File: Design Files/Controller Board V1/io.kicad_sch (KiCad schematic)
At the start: 16 parts, among them J1 XT30PW-F, J10 SM04B-GHS-TB_LF__SN_-, J11 SM04B-GHS-TB_LF__SN_-, J2 XT30UPB-M, J3 XT30UPB-M, J4 XT30UPB-M, J5 XT30UPB-M, J6 XT30UPB-M, J7 XT30UPB-M, J8 SM04B-GHS-TB_LF__SN_-, J9 SM04B-GHS-TB_LF__SN_-

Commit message: OOps, pushing late
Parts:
- J10, J11, J9: footprint SM04B-GHS-TB_LF__SN_-:JST_SM04B-GHS-TB_LF__SN_- -> PGA460TW:JST_SM04B-GHS-TB_LF__SN_-
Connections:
- net GPIO_0: now also J11.2; no longer J11.3
- net GPIO_1: now also J11.3; no longer J11.2
- net GPIO_2: now also J10.2; no longer J10.3
- net GPIO_3: now also J10.3; no longer J10.2
- net GPIO_4: now also J9.2; no longer J9.3
- net GPIO_5: now also J9.3; no longer J9.2
- net I2C_TypeC_SCL: now also J8.1; no longer J8.3
- net I2C_TypeC_SDA: now also J8.3; no longer J8.1
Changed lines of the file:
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@@
+		)
+	)
+	(hierarchical_label "GPIO_2"
+		(shape bidirectional)
+		(at 143.51 88.9 180)
+		(fields_autoplaced yes)
+		(effects
+			(font
+				(size 1.27 1.27)
+			)
+			(justify right)
 		)
 	)
@@
 		)
 	)
-	(hierarchical_label "GPIO_1"
-		(shape bidirectional)
-		(at 143.51 107.95 180)
-		(fields_autoplaced yes)
-		(effects
-			(font
-				(size 1.27 1.27)
-			)
-			(justify right)
-		)
-	)
-	(hierarchical_label "GPIO_0"
-		(shape bidirectional)
-		(at 143.51 110.49 180)
-		(fields_autoplaced yes)
-		(effects
-			(font
-				(size 1.27 1.27)
-			)
-			(justify right)
-		)
-	)
 	(hierarchical_label "24V_OUT"
 		(shape input)
@@
 		)
 	)
+	(hierarchical_label "GPIO_5"
+		(shape bidirectional)
+		(at 143.51 72.39 180)
+		(fields_autoplaced yes)
+		(effects
+			(font
+				(size 1.27 1.27)
+			)
+			(justify right)
+		)
+	)
 	(hierarchical_label "D_GND"
 		(shape input)
@@
 		)
 	)
-	(hierarchical_label "I2C_TypeC_SDA"
-		(shape input)
-		(at 143.51 48.26 180)
+	(hierarchical_label "GPIO_0"
+		(shape bidirectional)
+		(at 143.51 107.95 180)
 		(fields_autoplaced yes)
 		(effects
@@
 		)
 	)
-	(hierarchical_label "GPIO_2"
+	(hierarchical_label "GPIO_3"
 		(shape bidirectional)
 		(at 143.51 91.44 180)
@@
 		)
 	)
-	(hierarchical_label "GPIO_5"
-		(shape bidirectional)
-		(at 143.51 69.85 180)
-		(fields_autoplaced yes)
-		(effects
-			(font
-				(size 1.27 1.27)
-			)
-			(justify right)
-		)
-	)
-	(hierarchical_label "GPIO_3"
-		(shape bidirectional)
-		(at 143.51 88.9 180)
+	(hierarchical_label "I2C_TypeC_SCL"
+		(shape input)
+		(at 143.51 48.26 180)
 		(fields_autoplaced yes)
 		(effects
@@
 		)
 	)
+	(hierarchical_label "I2C_TypeC_SDA"
+		(shape input)
+		(at 143.51 53.34 180)
+		(fields_autoplaced yes)
+		(effects
+			(font
+				(size 1.27 1.27)
+			)
+			(justify right)
+		)
+	)
+	(hierarchical_label "GPIO_1"
+		(shape bidirectional)
+		(at 143.51 110.49 180)
+		(fields_autoplaced yes)
+		(effects
+			(font
+				(size 1.27 1.27)
+			)
+			(justify right)
+		)
+	)
 	(hierarchical_label "24_IN_PMM"
 		(shape input)
@@
 	(hierarchical_label "GPIO_4"
 		(shape bidirectional)
-		(at 143.51 72.39 180)
-		(fields_autoplaced yes)
-		(effects
-			(font
-				(size 1.27 1.27)
-			)
-			(justify right)
-		)
-	)
-	(hierarchical_label "I2C_TypeC_SCL"
-		(shape input)
-		(at 143.51 53.34 180)
+		(at 143.51 69.85 180)
 		(fields_autoplaced yes)
 		(effects
@@
 			)
 		)
-		(property "Footprint" "SM04B-GHS-TB_LF__SN_-:JST_SM04B-GHS-TB_LF__SN_-"
+		(property "Footprint" "PGA460TW:JST_SM04B-GHS-TB_LF__SN_-"
 			(at 153.67 91.44 0)
 			(effects
@@
 			)
 		)
-		(property "Footprint" "SM04B-GHS-TB_LF__SN_-:JST_SM04B-GHS-TB_LF__SN_-"
+		(property "Footprint" "PGA460TW:JST_SM04B-GHS-TB_LF__SN_-"
 			(at 153.67 110.49 0)
 			(effects
@@
 			)
 		)
-		(property "Footprint" "SM04B-GHS-TB_LF__SN_-:JST_SM04B-GHS-TB_LF__SN_-"
+		(property "Footprint" "PGA460TW:JST_SM04B-GHS-TB_LF__SN_-"
 			(at 153.67 72.39 0)
 			(effects

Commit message: board
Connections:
- net D_GND is gone; now on net P_GND: J10.4, J11.4, J8.2, J8.4, J9.4

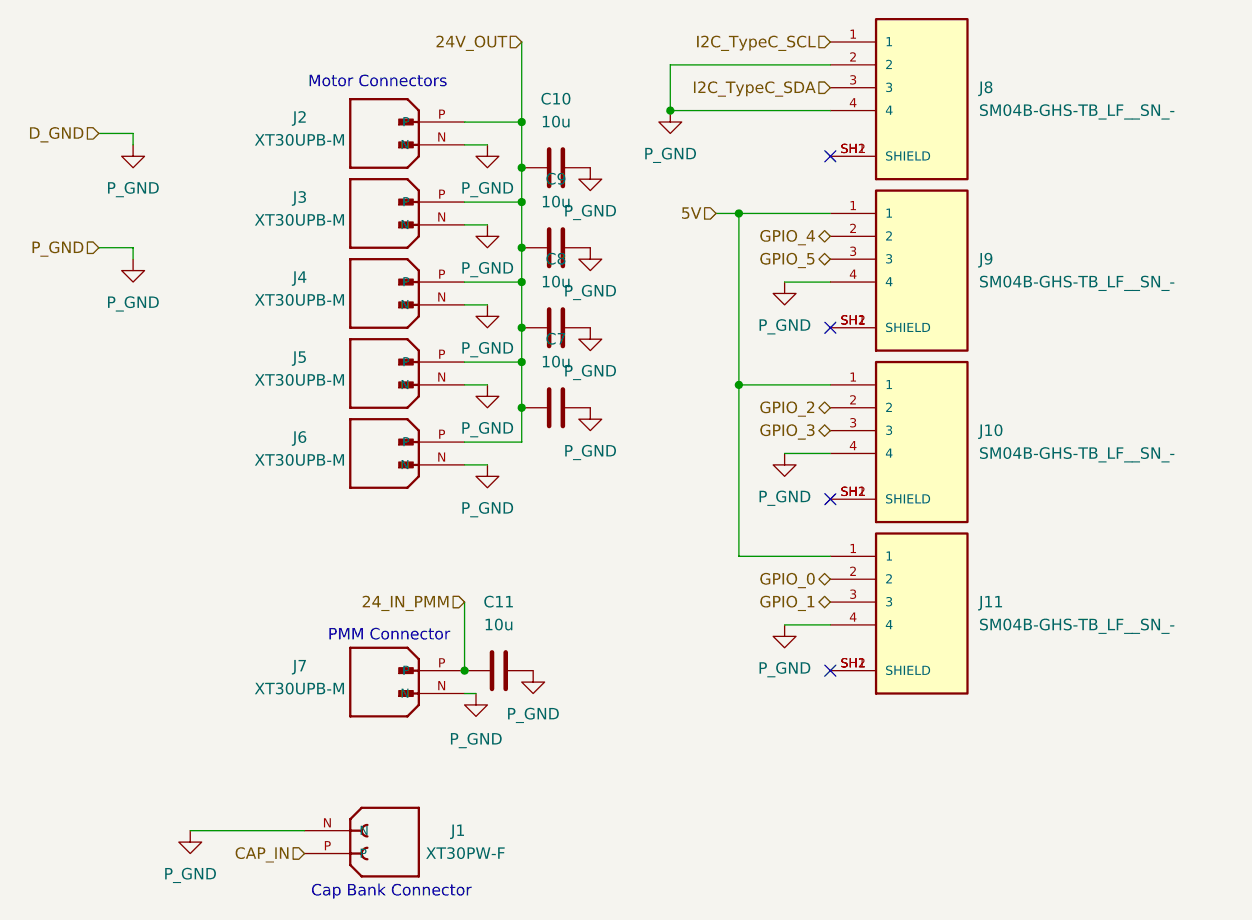
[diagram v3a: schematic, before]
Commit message: Added i2c level shifter
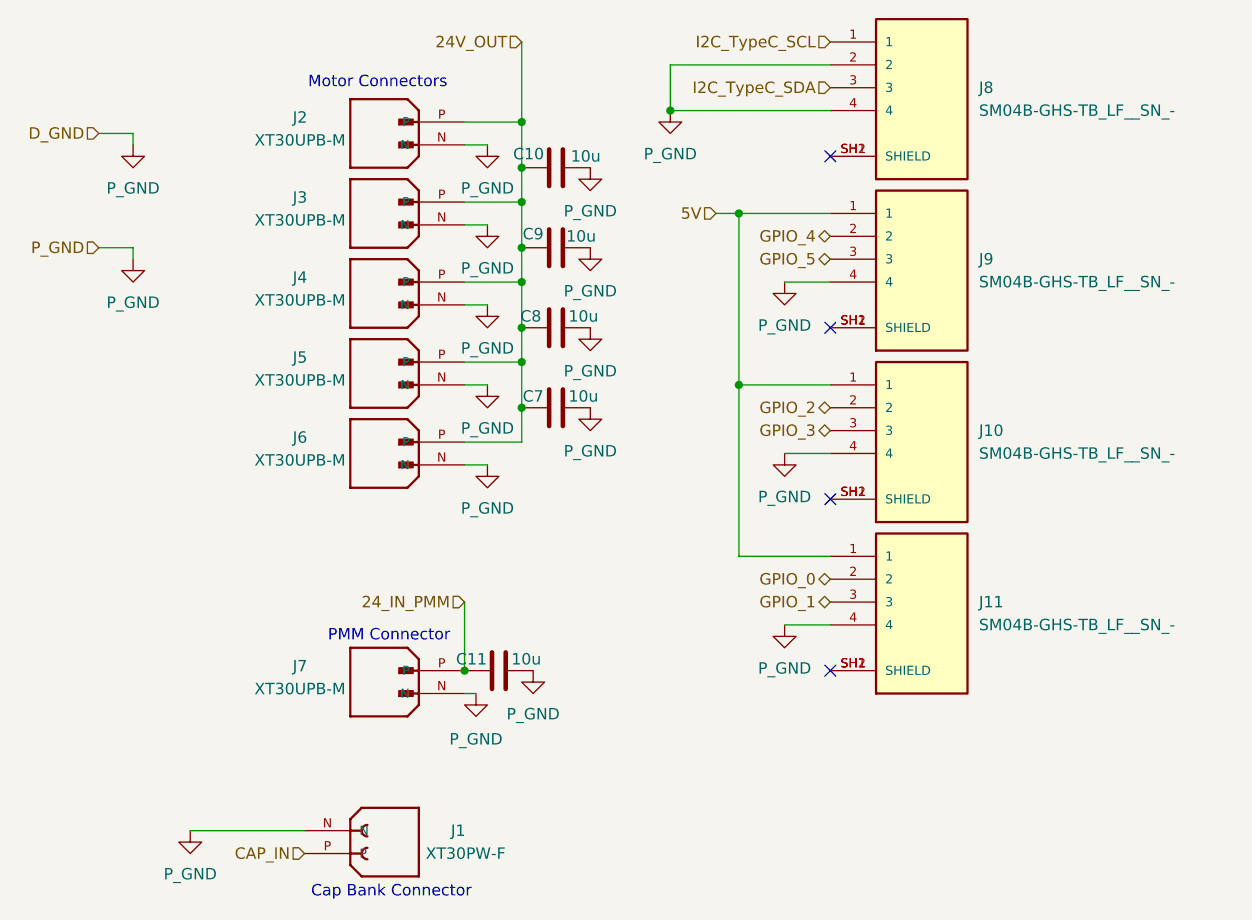
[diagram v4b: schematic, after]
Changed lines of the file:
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@@
 		(on_board yes)
 		(dnp no)
-		(fields_autoplaced yes)
 		(property "Reference" "C9"
-			(at 113.03 63.5 90)
+			(at 110.49 69.596 90)
 			(effects
 				(font
@@
 		)
 		(property "Value" "10u"
-			(at 113.03 66.04 90)
+			(at 115.824 69.85 90)
 			(effects
 				(font
@@
 		(on_board yes)
 		(dnp no)
-		(fields_autoplaced yes)
 		(property "Reference" "C8"
-			(at 113.03 72.39 90)
+			(at 110.236 78.74 90)
 			(effects
 				(font
@@
 		)
 		(property "Value" "10u"
-			(at 113.03 74.93 90)
+			(at 116.078 78.74 90)
 			(effects
 				(font
@@
 		(on_board yes)
 		(dnp no)
-		(fields_autoplaced yes)
 		(property "Reference" "C10"
-			(at 113.03 54.61 90)
+			(at 109.982 60.706 90)
 			(effects
 				(font
@@
 		)
 		(property "Value" "10u"
-			(at 113.03 57.15 90)
+			(at 116.332 60.96 90)
 			(effects
 				(font
@@
 		(on_board yes)
 		(dnp no)
-		(fields_autoplaced yes)
 		(property "Reference" "C7"
-			(at 113.03 81.28 90)
+			(at 110.49 87.63 90)
 			(effects
 				(font
@@
 		)
 		(property "Value" "10u"
-			(at 113.03 83.82 90)
+			(at 116.078 87.63 90)
 			(effects
 				(font
@@
 		(on_board yes)
 		(dnp no)
-		(fields_autoplaced yes)
 		(property "Reference" "C11"
-			(at 106.68 110.49 90)
+			(at 103.632 116.84 90)
 			(effects
 				(font
@@
 		)
 		(property "Value" "10u"
-			(at 106.68 113.03 90)
-			(effects
-				(font
+			(at 109.728 116.84 90)
+			(effects
+				(font

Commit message: half finished with brooks changes
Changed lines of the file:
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@@
+	)
+	(junction
+		(at 102.87 121.92)
+		(diameter 0)
+		(color 0 0 0 0)
 	)
 	(junction
@@
 	(wire
 		(pts
-			(xy 66.04 58.42) (xy 62.23 58.42)
-		)
-		(stroke
-			(width 0)
-			(type default)
-		)
-	)
-	(wire
-		(pts
 			(xy 102.87 83.82) (xy 109.22 83.82)
 		)
@@
 	(wire
 		(pts
-			(xy 66.04 71.12) (xy 66.04 72.39)
-		)
-		(stroke
-			(width 0)
-			(type default)
-		)
-	)
-	(wire
-		(pts
-			(xy 66.04 59.69) (xy 66.04 58.42)
-		)
-		(stroke
-			(width 0)
-			(type default)
-		)
-	)
-	(wire
-		(pts
 			(xy 105.41 68.58) (xy 102.87 68.58)
 		)
@@
 	(wire
 		(pts
+			(xy 102.87 121.92) (xy 102.87 120.65)
+		)
+		(stroke
+			(width 0)
+			(type default)
+		)
+	)
+	(wire
+		(pts
 			(xy 138.43 93.98) (xy 143.51 93.98)
 		)
@@
 	(wire
 		(pts
-			(xy 62.23 71.12) (xy 66.04 71.12)
+			(xy 102.87 121.92) (xy 102.87 125.73)
 		)
 		(stroke
@@
 	(wire
 		(pts
+			(xy 100.33 121.92) (xy 102.87 121.92)
+		)
+		(stroke
+			(width 0)
+			(type default)
+		)
+	)
+	(wire
+		(pts
 			(xy 133.35 86.36) (xy 133.35 67.31)
 		)
@@
 	(wire
 		(pts
-			(xy 104.14 120.65) (xy 102.87 120.65)
-		)
-		(stroke
-			(width 0)
-			(type default)
-		)
-	)
-	(wire
-		(pts
 			(xy 102.87 57.15) (xy 109.22 57.15)
 		)
@@
 		(pts
 			(xy 109.22 88.9) (xy 109.22 92.71)
+		)
+		(stroke
+			(width 0)
+			(type default)
+		)
+	)
+	(wire
+		(pts
+			(xy 100.33 121.92) (xy 100.33 124.46)
 		)
 		(stroke
@@
 			(font
 				(size 1.27 1.27)
+			)
+		)
+	)
+	(global_label "P_GND"
+		(shape input)
+		(at 73.66 135.89 90)
+		(fields_autoplaced yes)
+		(effects
+			(font
+				(size 1.27 1.27)
+			)
+			(justify left)
+		)
+		(property "Intersheetrefs" "${INTERSHEET_REFS}"
+			(at 73.66 126.7967 90)
+			(effects
+				(font
+					(size 1.27 1.27)
+				)
+				(justify left)
+				(hide yes)
+			)
+		)
+	)
+	(global_label "P_GND"
+		(shape input)
+		(at 102.87 125.73 0)
+		(fields_autoplaced yes)
+		(effects
+			(font
+				(size 1.27 1.27)
+			)
+			(justify left)
+		)
+		(property "Intersheetrefs" "${INTERSHEET_REFS}"
+			(at 111.9633 125.73 0)
+			(effects
+				(font
+					(size 1.27 1.27)
+				)
+				(justify left)
+				(hide yes)
 			)
 		)
@@
 		)
 	)
-	(hierarchical_label "P_GND"
-		(shape input)
-		(at 62.23 71.12 180)
-		(fields_autoplaced yes)
-		(effects
-			(font
-				(size 1.27 1.27)
-			)
-			(justify right)
-		)
-	)
 	(hierarchical_label "24V_OUT"
 		(shape input)
@@
 		(shape bidirectional)
 		(at 143.51 72.39 180)
-		(fields_autoplaced yes)
-		(effects
-			(font
-				(size 1.27 1.27)
-			)
-			(justify right)
-		)
-	)
-	(hierarchical_label "D_GND"
-		(shape input)
-		(at 62.23 58.42 180)
 		(fields_autoplaced yes)
 		(effects
@@
 	(symbol
 		(lib_id "power:GND")
-		(at 66.04 59.69 0)
-		(unit 1)
-		(exclude_from_sim no)
-		(in_bom yes)
-		(on_board yes)
-		(dnp no)
-		(property "Reference" "#PWR05"
-			(at 66.04 66.04 0)
-			(effects
-				(font
-					(size 1.27 1.27)
-				)
-				(hide yes)
-			)
-		)
-		(property "Value" "P_GND"
-			(at 66.04 64.516 0)
-			(effects
-				(font
-					(size 1.27 1.27)
-				)
-			)
-		)
-		(property "Footprint" ""
-			(at 66.04 59.69 0)
-			(effects
-				(font
-					(size 1.27 1.27)
-				)
-				(hide yes)
-			)
-		)
-		(property "Datasheet" ""
-			(at 66.04 59.69 0)
-			(effects
-				(font
-					(size 1.27 1.27)
-				)
-				(hide yes)
-			)
-		)
-		(property "Description" "Power symbol creates a global label with name \"GND\" , ground"
-			(at 66.04 59.69 0)
-			(effects
-				(font
-					(size 1.27 1.27)
-				)
-				(hide yes)
-			)
-		)
-		(pin "1"
-		)
-		(instances
-			(project "Control Board V1"
-				(path "/e0c606b8-cbb9-4aff-b96c-73876da6ca74/ba5c2d63-7c4b-497a-9de4-bddeb8ed5de8"
-					(reference "#PWR05")
-					(unit 1)
-				)
-			)
-		)
-	)
-	(symbol
-		(lib_id "power:GND")
 		(at 105.41 77.47 0)
 		(unit 1)
@@
 	(symbol
 		(lib_id "power:GND")
-		(at 104.14 120.65 0)
+		(at 100.33 124.46 0)
 		(unit 1)
 		(exclude_from_sim no)
@@
 		(dnp no)
 		(property "Reference" "#PWR026"
-			(at 104.14 127 0)
+			(at 100.33 130.81 0)
 			(effects
 				(font
@@
 		)
 		(property "Value" "P_GND"
-			(at 104.14 125.73 0)
+			(at 100.33 129.54 0)
 			(effects
 				(font
@@
 		)
 		(property "Footprint" ""
-			(at 104.14 120.65 0)
+			(at 100.33 124.46 0)
 			(effects
 				(font
@@
 		)
 		(property "Datasheet" ""
-			(at 104.14 120.65 0)
+			(at 100.33 124.46 0)
 			(effects
 				(font
@@
 		)
 		(property "Description" "Power symbol creates a global label with name \"GND\" , ground"
-			(at 104.14 120.65 0)
+			(at 100.33 124.46 0)
 			(effects
 				(font
@@
 					(unit 1)
 				)
-			)
-		)
-	)
-	(symbol
-		(lib_id "power:GND")
-		(at 66.04 72.39 0)
-		(unit 1)
-		(exclude_from_sim no)
-		(in_bom yes)
-		(on_board yes)
-		(dnp no)
-		(property "Reference" "#PWR020"
-			(at 66.04 78.74 0)
-			(effects
-				(font
-					(size 1.27 1.27)
-				)
-				(hide yes)
-			)
-		)
-		(property "Value" "P_GND"
-			(at 66.04 77.216 0)
-			(effects
-				(font
-					(size 1.27 1.27)
-				)
-			)
-		)
-		(property "Footprint" ""
-			(at 66.04 72.39 0)
-			(effects
-				(font
-					(size 1.27 1.27)
-				)
-				(hide yes)
-			)
-		)
-		(property "Datasheet" ""
-			(at 66.04 72.39 0)
-			(effects
-				(font
-					(size 1.27 1.27)
-				)
-				(hide yes)
-			)
-		)
-		(property "Description" "Power symbol creates a global label with name \"GND\" , ground"
-			(at 66.04 72.39 0)
-			(effects
-				(font
-					(size 1.27 1.27)
-				)
-				(hide yes)
-			)
-		)
-		(pin "1"
-		)
-		(instances
-			(project "Control Board V1"
-				(path "/e0c606b8-cbb9-4aff-b96c-73876da6ca74/ba5c2d63-7c4b-497a-9de4-bddeb8ed5de8"
-					(reference "#PWR020")
-					(unit 1)
-				)

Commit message: brooks changes in
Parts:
- added C13: 47u, Capacitor_SMD:C_2220_5750Metric, symbol Device:C
- C10, C7, C8, C9: value 10u -> 47u; footprint Capacitor_SMD:C_0603_1608Metric -> Capacitor_SMD:C_2220_5750Metric
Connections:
- net 24V_OUT: now also C13.2
- net P_GND: now also C13.1; no longer J10.4, J11.4, J8.2, J8.4, J9.4
- new net D_GND: J10.4, J11.4, J8.2, J8.4, J9.4
